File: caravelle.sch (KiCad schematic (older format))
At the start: 71 parts, among them J1 Conn_01x04, J2 Conn_01x02_Female, J3 Conn_01x04, J4 Conn_01x02_Female, J5 Conn_01x01, J6 Conn_01x01, K1 keyboard_parts_KEYSW, K10 keyboard_parts_KEYSW, K11 keyboard_parts_KEYSW, K12 keyboard_parts_KEYSW, K13 keyboard_parts_KEYSW, K14 keyboard_parts_KEYSW, K15 keyboard_parts_KEYSW, K16 keyboard_parts_KEYSW, K17 keyboard_parts_KEYSW, K18 keyboard_parts_KEYSW, K19 keyboard_parts_KEYSW, K2 keyboard_parts_KEYSW, K20 keyboard_parts_KEYSW, K21 keyboard_parts_KEYSW, K22 keyboard_parts_KEYSW, K23 keyboard_parts_KEYSW, K24 keyboard_parts_KEYSW, K25 keyboard_parts_KEYSW, K26 keyboard_parts_KEYSW, K27 keyboard_parts_KEYSW, K28 keyboard_parts_KEYSW, K29 keyboard_parts_KEYSW, K3 keyboard_parts_KEYSW, K30 keyboard_parts_KEYSW, K31 keyboard_parts_KEYSW, K32 keyboard_parts_KEYSW, K33 keyboard_parts_KEYSW, K34 keyboard_parts_KEYSW, K35 keyboard_parts_KEYSW, K36 keyboard_parts_KEYSW, K37 keyboard_parts_KEYSW, K38 keyboard_parts_KEYSW, K39 keyboard_parts_KEYSW, K4 keyboard_parts_KEYSW, K40 keyboard_parts_KEYSW, K41 keyboard_parts_KEYSW, K42 keyboard_parts_KEYSW, K43 keyboard_parts_KEYSW, K44 keyboard_parts_KEYSW, K45 keyboard_parts_KEYSW, K46 keyboard_parts_KEYSW, K47 keyboard_parts_KEYSW, K48 keyboard_parts_KEYSW, K5 keyboard_parts_KEYSW, K6 keyboard_parts_KEYSW, K7 keyboard_parts_KEYSW, K8 keyboard_parts_KEYSW, K9 keyboard_parts_KEYSW, SW1 SW_SPDT, SW2 SW_SPDT, SW3 RESET_SW, SW4 RESET_SW, U1 BL652_LEFT, U11 logo1, U12 logo2, U13 logo1, U2 hole, U3 hole, U4 hole, U5 BL652_RIGHT, U6 hole, U7 hole, U8 hole

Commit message: Change matrix wiring
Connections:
- net GND: no longer K1.1, K10.1, K11.1, K12.1, K13.1, K14.1, K15.1, K16.1, K17.1, K18.1, K19.1, K2.1, K20.1, K21.1, K22.1, K23.1, K24.1, K3.1, K4.1, K5.1, K6.1, K7.1, K8.1, K9.1
- net GNDA: no longer K25.1, K26.1, K27.1, K28.1, K29.1, K30.1, K31.1, K32.1, K33.1, K34.1, K35.1, K36.1, K37.1, K38.1, K39.1, K40.1, K41.1, K42.1, K43.1, K44.1, K45.1, K46.1, K47.1, K48.1
- net ROW: now reaches U1.25 (SIO_00)
- net ROW: now also K1.1, K10.1, K11.1, K12.1, K13.1, K14.1, K15.1, K16.1, K17.1, K18.1, K19.1, K2.1, K20.1, K21.1, K22.1, K23.1, K24.1, K3.1, K4.1, K5.1, K6.1, K7.1, K8.1, K9.1
- net ROW_R: now reaches U5.34 (SIO_29/AIN5)
- net ROW_R: now also K25.1, K26.1, K27.1, K28.1, K29.1, K30.1, K31.1, K32.1, K33.1, K34.1, K35.1, K36.1, K37.1, K38.1, K39.1, K40.1, K41.1, K42.1, K43.1, K44.1, K45.1, K46.1, K47.1, K48.1
- no-connect marks 15 -> 13
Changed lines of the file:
@@
-	1    0    0    -1
-$EndComp
-$Comp
-L power:GNDA #PWR020
-U 1 1 5BF26681
-P 5500 6750
-F 0 "#PWR020" H 5500 6500 50  0001 C CNN
-F 1 "GNDA" H 5505 6577 50  0000 C CNN
-F 2 "" H 5500 6750 50  0001 C CNN
-F 3 "" H 5500 6750 50  0001 C CNN
-	1    5500 6750
 	1    0    0    -1
 $EndComp
@@
 Text Label 6250 1750 0    60   ~ 0
 L14
-$Comp
-L power:GND #PWR06
-U 1 1 5B0C0A9D
-P 5500 2550
-F 0 "#PWR06" H 5500 2300 50  0001 C CNN
-F 1 "GND" H 5500 2400 50  0000 C CNN
-F 2 "" H 5500 2550 50  0001 C CNN
-F 3 "" H 5500 2550 50  0001 C CNN
-	1    5500 2550
-	1    0    0    -1
-$EndComp
 Wire Wire Line
 	2900 1300 3000 1300
@@
 	1    0    0    -1
 $EndComp
-NoConn ~ 1500 1700
 NoConn ~ 3500 2900
 NoConn ~ 3500 2800
@@
 	1    0    0    -1
 $EndComp
-NoConn ~ 3550 6500
 NoConn ~ 3550 6600
 NoConn ~ 3550 6700
@@
 Wire Wire Line
 	950  6200 950  6000
+Text Label 1500 1700 2    60   ~ 0
+ROW
+Text Label 5500 2550 0    60   ~ 0
+ROW
+Text Label 3550 6500 0    60   ~ 0
+ROW_R
+Text Label 5500 6750 0    60   ~ 0
+ROW_R
 $EndSCHEMATC

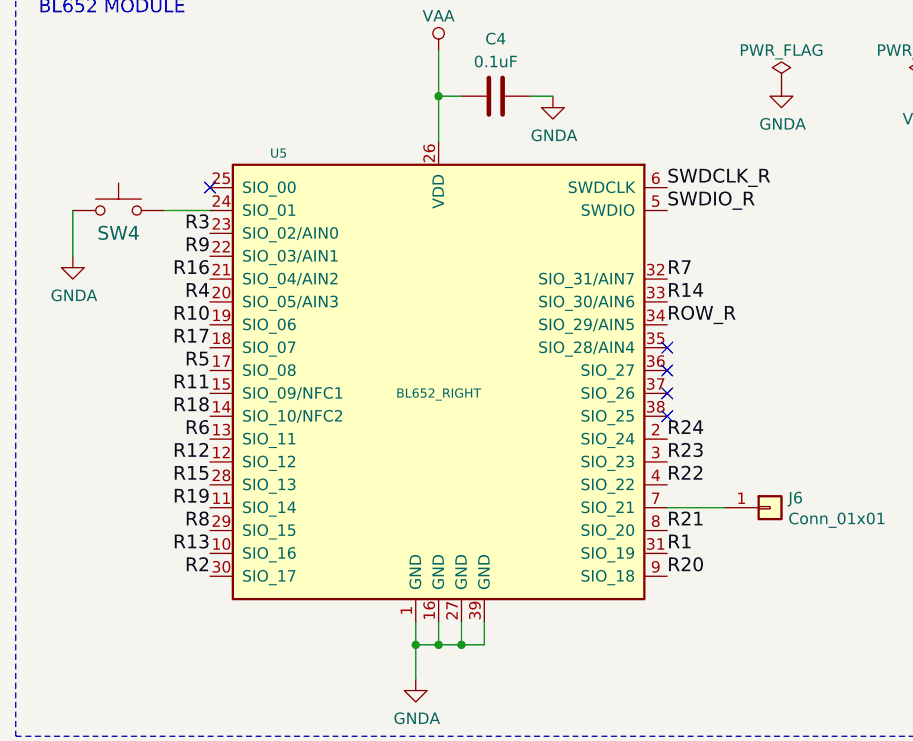
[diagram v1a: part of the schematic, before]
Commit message: Change matrix wiring
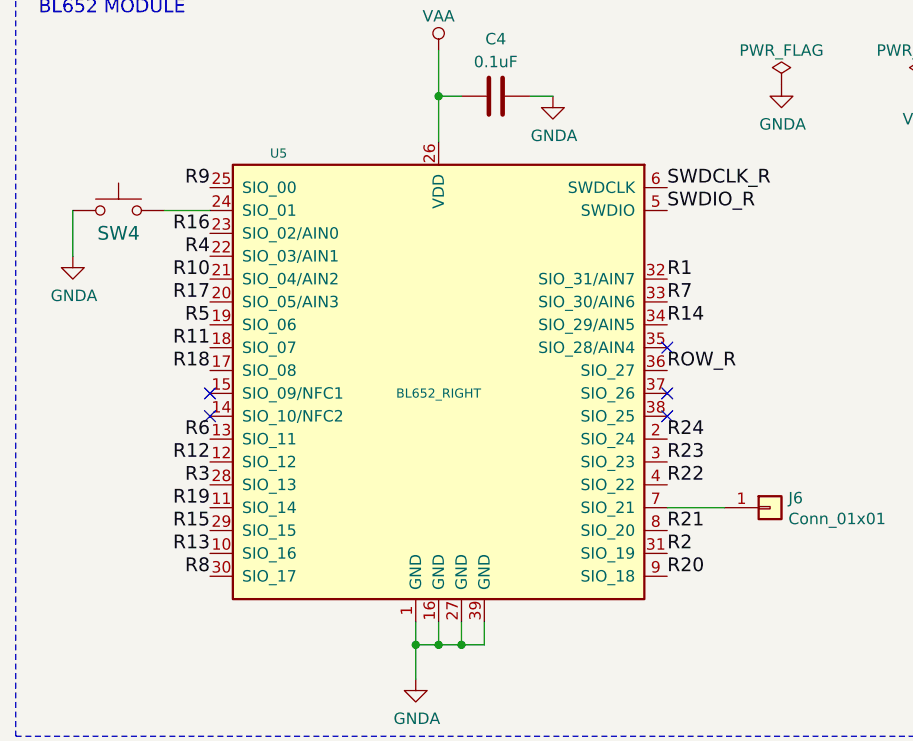
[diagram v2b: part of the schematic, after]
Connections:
- net R1: now also U5.32 (SIO_31/AIN7); no longer U5.31 (SIO_19)
- net R10: now also U5.21 (SIO_04/AIN2); no longer U5.19 (SIO_06)
- net R11: now also U5.18 (SIO_07); no longer U5.15 (SIO_09/NFC1)
- net R14: now also U5.34 (SIO_29/AIN5); no longer U5.33 (SIO_30/AIN6)
- net R15: now also U5.29 (SIO_15); no longer U5.28 (SIO_13)
- net R16: now also U5.23 (SIO_02/AIN0); no longer U5.21 (SIO_04/AIN2)
- net R17: now also U5.20 (SIO_05/AIN3); no longer U5.18 (SIO_07)
- net R18: now also U5.17 (SIO_08); no longer U5.14 (SIO_10/NFC2)
- net R2: now also U5.31 (SIO_19); no longer U5.30 (SIO_17)
- net R3: now also U5.28 (SIO_13); no longer U5.23 (SIO_02/AIN0)
- net R4: now also U5.22 (SIO_03/AIN1); no longer U5.20 (SIO_05/AIN3)
- net R5: now also U5.19 (SIO_06); no longer U5.17 (SIO_08)
- net R7: now also U5.33 (SIO_30/AIN6); no longer U5.32 (SIO_31/AIN7)
- net R8: now also U5.30 (SIO_17); no longer U5.29 (SIO_15)
- net R9: now also U5.25 (SIO_00); no longer U5.22 (SIO_03/AIN1)
- net ROW_R: now also U5.36 (SIO_27); no longer U5.34 (SIO_29/AIN5)
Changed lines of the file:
@@
 Wire Wire Line
 	1500 1800 1350 1800
-NoConn ~ 1550 5900
 Text Label 1550 7500 2    60   ~ 0
 R13
 Text Label 1550 7000 2    60   ~ 0
 R6
+Text Label 1550 6100 2    60   ~ 0
+R16
+Text Label 1550 5900 2    60   ~ 0
+R9
+Text Label 1550 7200 2    60   ~ 0
+R3
+Text Label 1550 6400 2    60   ~ 0
+R17
 Text Label 1550 6300 2    60   ~ 0
-R16
+R10
 Text Label 1550 6200 2    60   ~ 0
-R9
-Text Label 1550 6100 2    60   ~ 0
-R3
+R4
+Text Label 1550 7400 2    60   ~ 0
+R15
+Text Label 1550 7600 2    60   ~ 0
+R8
+Text Label 3550 7500 0    60   ~ 0
+R2
+Text Label 1550 6700 2    60   ~ 0
+R18
 Text Label 1550 6600 2    60   ~ 0
-R17
+R11
 Text Label 1550 6500 2    60   ~ 0
-R10
-Text Label 1550 6400 2    60   ~ 0
-R4
-Text Label 1550 7200 2    60   ~ 0
-R15
-Text Label 1550 7400 2    60   ~ 0
-R8
-Text Label 1550 7600 2    60   ~ 0
-R2
-Text Label 1550 6900 2    60   ~ 0
-R18
-Text Label 1550 6800 2    60   ~ 0
-R11
-Text Label 1550 6700 2    60   ~ 0
 R5
 Text Label 1550 7300 2    60   ~ 0
@@
 Text Label 3550 5900 0    60   ~ 0
 SWDCLK_R
-Text Label 3550 7500 0    60   ~ 0
+Text Label 3550 6300 0    60   ~ 0
 R1
 Text Label 3550 7000 0    60   ~ 0
@@
 Wire Wire Line
 	2550 5500 2650 5500
-Text Label 3550 6300 0    60   ~ 0
+Text Label 3550 6400 0    60   ~ 0
 R7
-Text Label 3550 6400 0    60   ~ 0
+Text Label 3550 6500 0    60   ~ 0
 R14
 Text Label 3550 7600 0    60   ~ 0
@@
 	1    0    0    -1
 $EndComp
-NoConn ~ 3550 6600
-NoConn ~ 3550 6700
 NoConn ~ 3550 6800
 NoConn ~ 3550 6900
@@
 Text Label 5500 2550 0    60   ~ 0
 ROW
-Text Label 3550 6500 0    60   ~ 0
+Text Label 3550 6700 0    60   ~ 0
 ROW_R
 Text Label 5500 6750 0    60   ~ 0
 ROW_R
+NoConn ~ 1550 6800
+NoConn ~ 1550 6900
+NoConn ~ 3550 6600
 $EndSCHEMATC

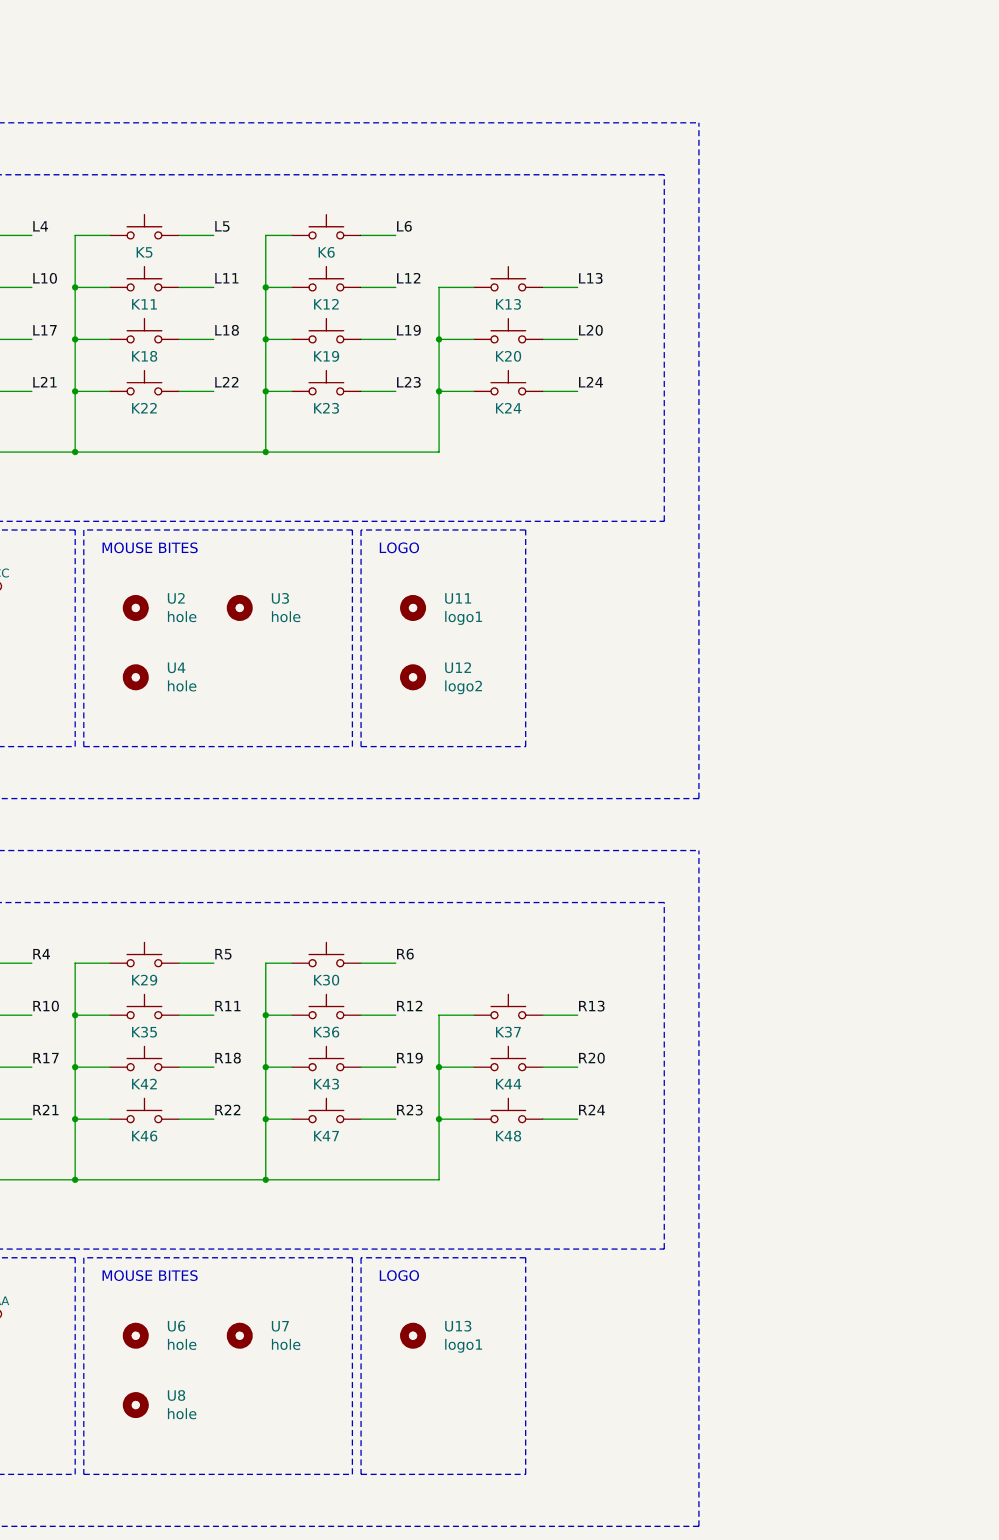
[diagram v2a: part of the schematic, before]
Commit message: Add edge rails for PCBA
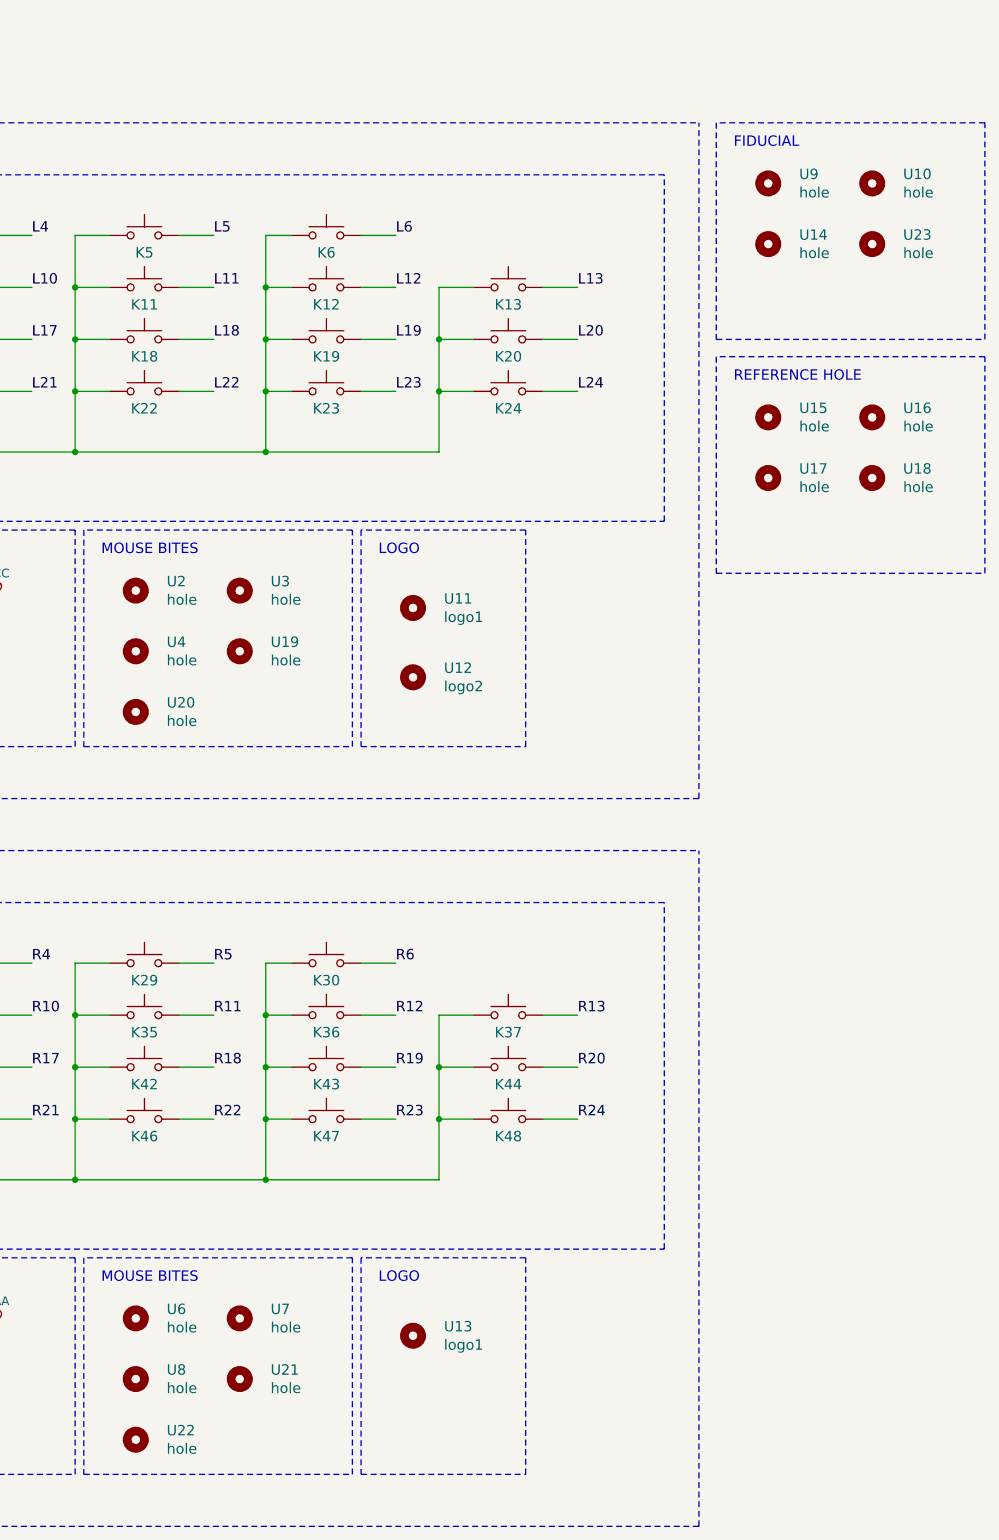
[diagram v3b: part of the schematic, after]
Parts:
- added U10, U9: hole, Fiducial:Fiducial_1mm_Mask3mm, symbol Mechanical:MountingHole
- added U14, U23: hole, Fiducial:Fiducial_0.75mm_Mask2.25mm, symbol Mechanical:MountingHole
- added U15, U16, U17, U18: hole, MountingHole:MountingHole_4mm, symbol Mechanical:MountingHole
- added U19, U20, U21, U22: hole, random-keyboard-parts:breakaway-mousebites, symbol Mechanical:MountingHole
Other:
- note added: "FIDUCIAL"
- note added: "REFERENCE HOLE"
- moved on the sheet: U2, U3, U4, U6, U7, U8
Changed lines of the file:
@@
 L Mechanical:MountingHole U2
 U 1 1 5CAC27DC
-P 10100 3300
-F 0 "U2" H 10278 3353 60  0000 L CNN
-F 1 "hole" H 10278 3247 60  0000 L CNN
-F 2 "random-keyboard-parts:breakaway-mousebites" H 10100 3300 60  0001 C CNN
-F 3 "" H 10100 3300 60  0001 C CNN
-	1    10100 3300
+P 10100 3200
+F 0 "U2" H 10278 3253 60  0000 L CNN
+F 1 "hole" H 10278 3147 60  0000 L CNN
+F 2 "random-keyboard-parts:breakaway-mousebites" H 10100 3200 60  0001 C CNN
+F 3 "" H 10100 3200 60  0001 C CNN
+	1    10100 3200
 	1    0    0    -1
 $EndComp
@@
 L Mechanical:MountingHole U3
 U 1 1 5CAFE7E6
-P 10700 3300
-F 0 "U3" H 10878 3353 60  0000 L CNN
-F 1 "hole" H 10878 3247 60  0000 L CNN
-F 2 "random-keyboard-parts:breakaway-mousebites" H 10700 3300 60  0001 C CNN
-F 3 "" H 10700 3300 60  0001 C CNN
-	1    10700 3300
+P 10700 3200
+F 0 "U3" H 10878 3253 60  0000 L CNN
+F 1 "hole" H 10878 3147 60  0000 L CNN
+F 2 "random-keyboard-parts:breakaway-mousebites" H 10700 3200 60  0001 C CNN
+F 3 "" H 10700 3200 60  0001 C CNN
+	1    10700 3200
 	1    0    0    -1
 $EndComp
@@
 L Mechanical:MountingHole U6
 U 1 1 5CAFF053
-P 10100 7500
-F 0 "U6" H 10278 7553 60  0000 L CNN
-F 1 "hole" H 10278 7447 60  0000 L CNN
-F 2 "random-keyboard-parts:breakaway-mousebites" H 10100 7500 60  0001 C CNN
-F 3 "" H 10100 7500 60  0001 C CNN
-	1    10100 7500
+P 10100 7400
+F 0 "U6" H 10278 7453 60  0000 L CNN
+F 1 "hole" H 10278 7347 60  0000 L CNN
+F 2 "random-keyboard-parts:breakaway-mousebites" H 10100 7400 60  0001 C CNN
+F 3 "" H 10100 7400 60  0001 C CNN
+	1    10100 7400
 	1    0    0    -1
 $EndComp
@@
 L Mechanical:MountingHole U7
 U 1 1 5CAFF064
-P 10700 7500
-F 0 "U7" H 10878 7553 60  0000 L CNN
-F 1 "hole" H 10878 7447 60  0000 L CNN
-F 2 "random-keyboard-parts:breakaway-mousebites" H 10700 7500 60  0001 C CNN
-F 3 "" H 10700 7500 60  0001 C CNN
-	1    10700 7500
+P 10700 7400
+F 0 "U7" H 10878 7453 60  0000 L CNN
+F 1 "hole" H 10878 7347 60  0000 L CNN
+F 2 "random-keyboard-parts:breakaway-mousebites" H 10700 7400 60  0001 C CNN
+F 3 "" H 10700 7400 60  0001 C CNN
+	1    10700 7400
 	1    0    0    -1
 $EndComp
@@
 L Mechanical:MountingHole U4
 U 1 1 5CAD1F0F
-P 10100 3700
-F 0 "U4" H 10278 3753 60  0000 L CNN
-F 1 "hole" H 10278 3647 60  0000 L CNN
-F 2 "random-keyboard-parts:breakaway-mousebites" H 10100 3700 60  0001 C CNN
-F 3 "" H 10100 3700 60  0001 C CNN
-	1    10100 3700
+P 10100 3550
+F 0 "U4" H 10278 3603 60  0000 L CNN
+F 1 "hole" H 10278 3497 60  0000 L CNN
+F 2 "random-keyboard-parts:breakaway-mousebites" H 10100 3550 60  0001 C CNN
+F 3 "" H 10100 3550 60  0001 C CNN
+	1    10100 3550
 	1    0    0    -1
 $EndComp
@@
 L Mechanical:MountingHole U8
 U 1 1 5CAE0D14
-P 10100 7900
-F 0 "U8" H 10278 7953 60  0000 L CNN
-F 1 "hole" H 10278 7847 60  0000 L CNN
-F 2 "random-keyboard-parts:breakaway-mousebites" H 10100 7900 60  0001 C CNN
-F 3 "" H 10100 7900 60  0001 C CNN
-	1    10100 7900
+P 10100 7750
+F 0 "U8" H 10278 7803 60  0000 L CNN
+F 1 "hole" H 10278 7697 60  0000 L CNN
+F 2 "random-keyboard-parts:breakaway-mousebites" H 10100 7750 60  0001 C CNN
+F 3 "" H 10100 7750 60  0001 C CNN
+	1    10100 7750
 	1    0    0    -1
 $EndComp
@@
 NoConn ~ 1550 6900
 NoConn ~ 3550 6600
+$Comp
+L Mechanical:MountingHole U19
+U 1 1 5E020BCB
+P 10700 3550
+F 0 "U19" H 10878 3603 60  0000 L CNN
+F 1 "hole" H 10878 3497 60  0000 L CNN
+F 2 "random-keyboard-parts:breakaway-mousebites" H 10700 3550 60  0001 C CNN
+F 3 "" H 10700 3550 60  0001 C CNN
+	1    10700 3550
+	1    0    0    -1
+$EndComp
+$Comp
+L Mechanical:MountingHole U20
+U 1 1 5E021619
+P 10100 3900
+F 0 "U20" H 10278 3953 60  0000 L CNN
+F 1 "hole" H 10278 3847 60  0000 L CNN
+F 2 "random-keyboard-parts:breakaway-mousebites" H 10100 3900 60  0001 C CNN
+F 3 "" H 10100 3900 60  0001 C CNN
+	1    10100 3900
+	1    0    0    -1
+$EndComp
+$Comp
+L Mechanical:MountingHole U21
+U 1 1 5E040166
+P 10700 7750
+F 0 "U21" H 10878 7803 60  0000 L CNN
+F 1 "hole" H 10878 7697 60  0000 L CNN
+F 2 "random-keyboard-parts:breakaway-mousebites" H 10700 7750 60  0001 C CNN
+F 3 "" H 10700 7750 60  0001 C CNN
+	1    10700 7750
+	1    0    0    -1
+$EndComp
+$Comp
+L Mechanical:MountingHole U22
+U 1 1 5E04041A
+P 10100 8100
+F 0 "U22" H 10278 8153 60  0000 L CNN
+F 1 "hole" H 10278 8047 60  0000 L CNN
+F 2 "random-keyboard-parts:breakaway-mousebites" H 10100 8100 60  0001 C CNN
+F 3 "" H 10100 8100 60  0001 C CNN
+	1    10100 8100
+	1    0    0    -1
+$EndComp
+$Comp
+L Mechanical:MountingHole U9
+U 1 1 5E044C5A
+P 13750 850
+F 0 "U9" H 13928 903 60  0000 L CNN
+F 1 "hole" H 13928 797 60  0000 L CNN
+F 2 "Fiducial:Fiducial_1mm_Mask3mm" H 13750 850 60  0001 C CNN
+F 3 "" H 13750 850 60  0001 C CNN
+	1    13750 850
+	1    0    0    -1
+$EndComp
+Wire Notes Line
+	15000 1750 15000 500
+Text Notes 13550 650  0    60   ~ 0
+FIDUCIAL
+Wire Notes Line
+	13450 1750 15000 1750
+Wire Notes Line
+	15000 500  13450 500
+Wire Notes Line
+	13450 500  13450 1750
+$Comp
+L Mechanical:MountingHole U10
+U 1 1 5E044C69
+P 14350 850
+F 0 "U10" H 14528 903 60  0000 L CNN
+F 1 "hole" H 14528 797 60  0000 L CNN
+F 2 "Fiducial:Fiducial_1mm_Mask3mm" H 14350 850 60  0001 C CNN
+F 3 "" H 14350 850 60  0001 C CNN
+	1    14350 850
+	1    0    0    -1
+$EndComp
+$Comp
+L Mechanical:MountingHole U14
+U 1 1 5E044C73
+P 13750 1200
+F 0 "U14" H 13928 1253 60  0000 L CNN
+F 1 "hole" H 13928 1147 60  0000 L CNN
+F 2 "Fiducial:Fiducial_0.75mm_Mask2.25mm" H 13750 1200 60  0001 C CNN
+F 3 "" H 13750 1200 60  0001 C CNN
+	1    13750 1200
+	1    0    0    -1
+$EndComp
+$Comp
+L Mechanical:MountingHole U15
+U 1 1 5E0580A4
+P 13750 2200
+F 0 "U15" H 13928 2253 60  0000 L CNN
+F 1 "hole" H 13928 2147 60  0000 L CNN
+F 2 "MountingHole:MountingHole_4mm" H 13750 2200 60  0001 C CNN
+F 3 "" H 13750 2200 60  0001 C CNN
+	1    13750 2200
+	1    0    0    -1
+$EndComp
+Wire Notes Line
+	15000 3100 15000 1850
+Wire Notes Line
+	13450 3100 15000 3100
+Wire Notes Line
+	15000 1850 13450 1850
+Wire Notes Line
+	13450 1850 13450 3100
+$Comp
+L Mechanical:MountingHole U16
+U 1 1 5E0580B3
+P 14350 2200
+F 0 "U16" H 14528 2253 60  0000 L CNN
+F 1 "hole" H 14528 2147 60  0000 L CNN
+F 2 "MountingHole:MountingHole_4mm" H 14350 2200 60  0001 C CNN
+F 3 "" H 14350 2200 60  0001 C CNN
+	1    14350 2200
+	1    0    0    -1
+$EndComp
+$Comp
+L Mechanical:MountingHole U17
+U 1 1 5E0580BD
+P 13750 2550
+F 0 "U17" H 13928 2603 60  0000 L CNN
+F 1 "hole" H 13928 2497 60  0000 L CNN
+F 2 "MountingHole:MountingHole_4mm" H 13750 2550 60  0001 C CNN
+F 3 "" H 13750 2550 60  0001 C CNN
+	1    13750 2550
+	1    0    0    -1
+$EndComp
+$Comp
+L Mechanical:MountingHole U18
+U 1 1 5E0580C7
+P 14350 2550
+F 0 "U18" H 14528 2603 60  0000 L CNN
+F 1 "hole" H 14528 2497 60  0000 L CNN
+F 2 "MountingHole:MountingHole_4mm" H 14350 2550 60  0001 C CNN
+F 3 "" H 14350 2550 60  0001 C CNN
+	1    14350 2550
+	1    0    0    -1
+$EndComp
+$Comp
+L Mechanical:MountingHole U23
+U 1 1 5E044C7D
+P 14350 1200
+F 0 "U23" H 14528 1253 60  0000 L CNN
+F 1 "hole" H 14528 1147 60  0000 L CNN
+F 2 "Fiducial:Fiducial_0.75mm_Mask2.25mm" H 14350 1200 60  0001 C CNN
+F 3 "" H 14350 1200 60  0001 C CNN
+	1    14350 1200
+	1    0    0    -1
+$EndComp
+Text Notes 13550 2000 0    60   ~ 0
+REFERENCE HOLE
 $EndSCHEMATC

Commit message: Clean up Fab
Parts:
- U10, U14, U23, U9: value hole -> fiducial
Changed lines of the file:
@@
 P 13750 850
 F 0 "U9" H 13928 903 60  0000 L CNN
-F 1 "hole" H 13928 797 60  0000 L CNN
+F 1 "fiducial" H 13928 797 60  0000 L CNN
 F 2 "Fiducial:Fiducial_1mm_Mask3mm" H 13750 850 60  0001 C CNN
 F 3 "" H 13750 850 60  0001 C CNN
@@
 P 14350 850
 F 0 "U10" H 14528 903 60  0000 L CNN
-F 1 "hole" H 14528 797 60  0000 L CNN
+F 1 "fiducial" H 14528 797 60  0000 L CNN
 F 2 "Fiducial:Fiducial_1mm_Mask3mm" H 14350 850 60  0001 C CNN
 F 3 "" H 14350 850 60  0001 C CNN
@@
 P 13750 1200
 F 0 "U14" H 13928 1253 60  0000 L CNN
-F 1 "hole" H 13928 1147 60  0000 L CNN
+F 1 "fiducial" H 13928 1147 60  0000 L CNN
 F 2 "Fiducial:Fiducial_0.75mm_Mask2.25mm" H 13750 1200 60  0001 C CNN
 F 3 "" H 13750 1200 60  0001 C CNN
@@
 P 14350 1200
 F 0 "U23" H 14528 1253 60  0000 L CNN
-F 1 "hole" H 14528 1147 60  0000 L CNN
+F 1 "fiducial" H 14528 1147 60  0000 L CNN
 F 2 "Fiducial:Fiducial_0.75mm_Mask2.25mm" H 14350 1200 60  0001 C CNN
 F 3 "" H 14350 1200 60  0001 C CNN

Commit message: Add Kailh hotswap footprint
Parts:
- K1, K10, K11, K12, K13, K14, K15, K16, K17, K18, K19, K2, K20, K23, K25, K26, K27, K28, K29, K3, K30, K31, K32, K33, K34, K35, K36, K37, K38, K39, K4, K40, K41, K42, K43, K44, K47, K5, K6, K7, K8, K9: footprint MX_Only:MXOnly-1U-NoLED -> MX_Only:MXOnly-1U-Hotswap-Antishear
- K21, K22, K45, K46: footprint MX_Only:MXOnly-1.25U-NoLED -> MX_Only:MXOnly-1U-Hotswap-Antishear
- K24, K48: footprint MX_Only:MXOnly-1.5U-NoLED -> MX_Only:MXOnly-1U-Hotswap-Antishear
